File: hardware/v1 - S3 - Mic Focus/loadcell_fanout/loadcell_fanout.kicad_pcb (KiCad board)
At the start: 2 copper layers, 20 x 100 mm, 18 parts, among them J1 Conn_01x05, J2 EXP, U2 L, U3 R

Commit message: WIP
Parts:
- moved FB1 2.50 mm to (176.5, 127.5), turned to 180 degrees
- moved J2 0.95 mm to (170.0, 120.0), turned to 90 degrees
- moved C1 0.28 mm to (176.5, 129.5), turned to 180 degrees
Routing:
- net /PDM_CLK: track 84.6 -> 92.6 mm
- net /I2C_SDA: track 20.2 -> 27.9 mm, vias 0 -> 1
- net /INT: track 20.3 -> 25.9 mm
- net Net-(J2-Pin_2): track 5.21 -> 8.67 mm, vias 1 -> 0
- net /PDM_D0: track 87.4 -> 84.8 mm
- net /I2C_SCL: track 23.3 -> 25.4 mm, vias 0 -> 1
- net GND: vias 0 -> 5

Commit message: WIP, standoffs
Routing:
- net GND: vias 5 -> 9
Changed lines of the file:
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@@
+	)
+	(via
+		(at 163 99)
+		(size 0.6)
+		(drill 0.3)
+		(layers "F.Cu" "B.Cu")
+		(net "GND")
 	)
 	(via
@@
 	)
 	(via
+		(at 173.5 123.5)
+		(size 0.6)
+		(drill 0.3)
+		(layers "F.Cu" "B.Cu")
+		(net "GND")
+	)
+	(via
 		(at 165.5 69)
 		(size 0.6)
@@
 	)
 	(via
+		(at 173.5 132.5)
+		(size 0.6)
+		(drill 0.3)
+		(layers "F.Cu" "B.Cu")
+		(net "GND")
+	)
+	(via
 		(at 163 67.5)
+		(size 0.6)
+		(drill 0.3)
+		(layers "F.Cu" "B.Cu")
+		(net "GND")
+	)
+	(via
+		(at 163 79)
 		(size 0.6)
 		(drill 0.3)
@@
 	)
 	(segment
-		(start 176.5 128.27)
-		(end 176.495 128.275)
-		(width 0.2)
-		(layer "F.Cu")
-		(net "+3.3V")
-	)
-	(segment
 		(start 173.5 99)
 		(end 173.5 95.8)
@@
 		(hatch edge 0.5)
 		(connect_pads
-			(clearance 0.5)
+			(clearance 0.2)
 		)
-		(min_thickness 0.25)
+		(min_thickness 0.2)
 		(fill yes
-			(thermal_gap 0.5)
-			(thermal_bridge_width 0.5)
+			(thermal_gap 0.2)
+			(thermal_bridge_width 0.2)
 			(island_removal_mode 0)
 		)

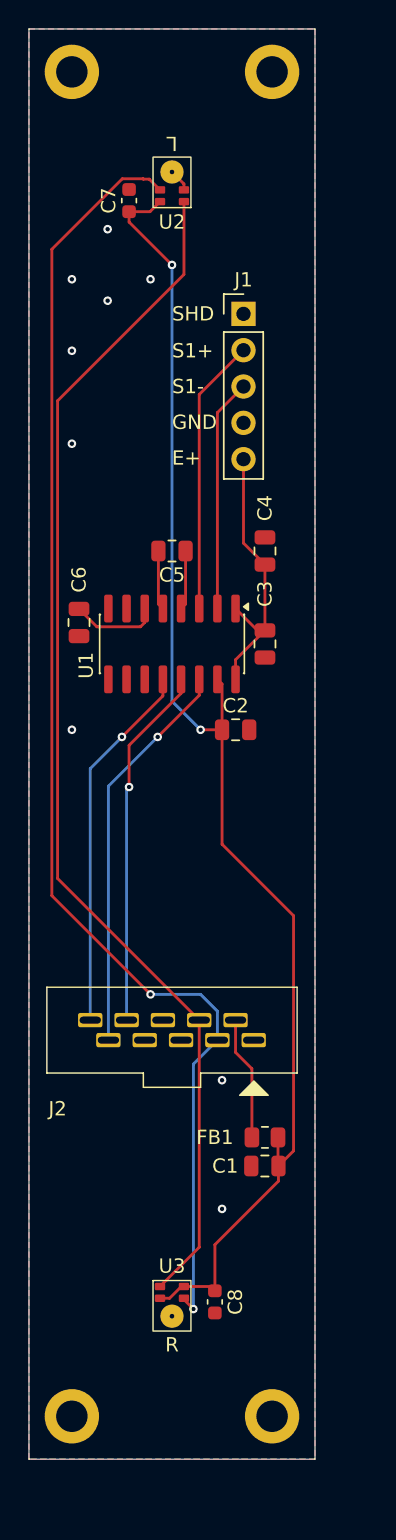
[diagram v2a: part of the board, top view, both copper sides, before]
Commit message: Standoff move, silkscreen work
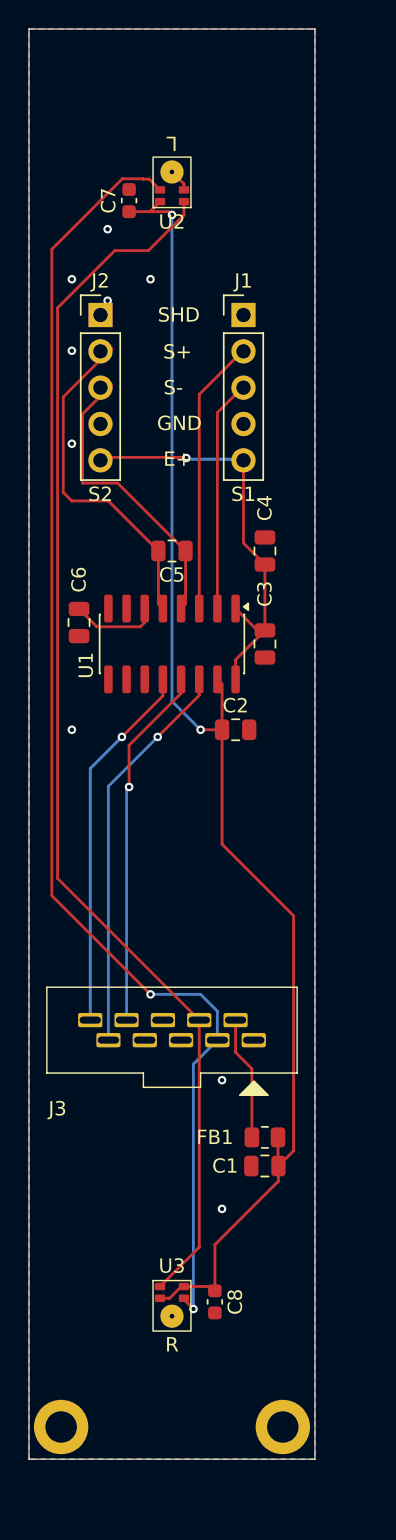
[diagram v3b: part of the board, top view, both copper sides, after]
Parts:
- removed the H1 at (163.0, 53.0)
- removed the H2 at (177.0, 53.0)
- added G***: LOGO, BVH_Logos:SkyIron_logo_Back, F.Cu at (170.5, 92.2)
- added J2: S2, Connector_PinHeader_2.54mm:PinHeader_1x05_P2.54mm_Vertical, F.Cu at (165.0, 70.0)
- J1: value Conn_01x05 -> S1
- moved H1 1.06 mm to (162.2, 147.8)
- moved H2 1.06 mm to (177.8, 147.8)
- moved J1 0.08 mm to (175.0, 70.0)
- renumbered H3 to H1, H4 to H2, J2 to J3
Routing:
- net /S2_P: track 4.16 -> 24.0 mm
- net /S2_N: track 4.16 -> 21.3 mm
- net /E_p: track 19.6 -> 28.6 mm, vias 0 -> 1
- net /PDM_D0: track 84.8 -> 86.1 mm
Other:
- copper layers 2 -> 4
- board text added: "${BOARD_DATE} - ${BOARD_REV}"
- board text added: "${BOARD_NAME}"
- board text added: "${OWNER}"
- board text added: "S+"
- board text added: "S-"
- board text removed: "AB4EN 2026-09-21 NAU7802 Breakout v1 2x PDM Microphones on D0"
- board text removed: "S1+"
- board text removed: "S1-"
